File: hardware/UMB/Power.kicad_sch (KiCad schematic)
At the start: 15 parts, among them U3 TLV743P, U4 MC78M12CDTG, U5 LM1117IMP-5.0

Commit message: Power section done
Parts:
- removed C13, C14, C16, C17: 1u, Capacitor_SMD:C_0603_1608Metric_Pad1.08x0.95mm_HandSolder, symbol Device:C
- removed C18: 100n, Capacitor_SMD:C_0603_1608Metric_Pad1.08x0.95mm_HandSolder, symbol Device:C
- removed F1: 500mA, Diode_SMD:D_1812_4532Metric_Pad1.30x3.40mm_HandSolder, symbol Device:Fuse
- removed U4: MC78M12CDTG, Package_TO_SOT_SMD:TO-252-3_TabPin2, symbol mc78m05_to252-regulator_linear:MC78M05_TO252-Regulator_Linear
- removed U5: LM1117IMP-5.0, Package_TO_SOT_SMD:SOT-223-3_TabPin2, symbol lm1117-5.0-regulator_linear:LM1117-5.0-Regulator_Linear
- added C14, C17, C18: 100n, Capacitor_SMD:C_0603_1608Metric_Pad1.08x0.95mm_HandSolder, symbol Device:C_Small
- added C16, C20, C29, C31, C41: 22u, Capacitor_SMD:C_0603_1608Metric_Pad1.08x0.95mm_HandSolder, symbol Device:C_Small
- added C19, C21, C42, C43: 10u, 10uFpolarized_cap:CAPAE660X600N, symbol Device:C_Polarized_Small
- added C22, C24, C26, C27: 2.2u, Capacitor_SMD:C_0805_2012Metric_Pad1.18x1.45mm_HandSolder, symbol Device:C_Small
- added C23: 8.2n, Capacitor_SMD:C_0603_1608Metric_Pad1.08x0.95mm_HandSolder, symbol Device:C_Small
- added C25, C30: 10u, Capacitor_SMD:C_0805_2012Metric_Pad1.18x1.45mm_HandSolder, symbol Device:C_Small
- added C28: 470n, Capacitor_SMD:C_0603_1608Metric_Pad1.08x0.95mm_HandSolder, symbol Device:C_Small
- added L1: 15uH, Inductor_SMD:L_APV_APH1040, symbol Device:L
- added L2: 6.8uH, inductor:VLS5045EX330M, symbol Device:L
- added R10, R13, R56: 10.2k, Resistor_SMD:R_0603_1608Metric_Pad0.98x0.95mm_HandSolder, symbol Device:R_Small
- added R12: 84.5k, Resistor_SMD:R_0603_1608Metric_Pad0.98x0.95mm_HandSolder, symbol Device:R_Small
- added R9: 174k, Resistor_SMD:R_0603_1608Metric_Pad0.98x0.95mm_HandSolder, symbol Device:R_Small
- added U4: TPS563300DRLR, sot-583-8:TPS62932DRLR, symbol TPS563300DRLR:TPS563300DRLR
- added U5: TPS563219ADDFR, SOT65P280X110-8N, symbol TPS563219ADDFR:TPS563219ADDFR
- added U6: AP2127N3-1.5, Package_TO_SOT_SMD:TSOT-23_HandSoldering, symbol Regulator_Linear:AP2127N3-1.5
- added U7: LDK320ADU120R, Package_TO_SOT_SMD:SOT-89-3_Handsoldering, symbol Regulator_Linear:L78L12_SOT89
- added U8: LM2940SX-12_NOPB, KTT0003B, symbol LM2940SX-12_NOPB:LM2940SX-12_NOPB
- added U9: LM1117IMP-5.0, Package_TO_SOT_SMD:SOT-223-3_TabPin2, symbol lm1117-5.0-regulator_linear:LM1117-5.0-Regulator_Linear
- C15: footprint Capacitor_SMD:C_0603_1608Metric -> Capacitor_SMD:C_0603_1608Metric_Pad1.08x0.95mm_HandSolder; Mouser (none) -> https://www.mouser.pl/ProductDetail/KEMET/C0603C104M4RACAUT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; Mouser No (none) -> 80-C0603C104M4RAUTO
- C32: renamed from C19; footprint Capacitor_SMD:C_0603_1608Metric -> Capacitor_SMD:C_0603_1608Metric_Pad1.08x0.95mm_HandSolder; Mouser (none) -> https://www.mouser.pl/ProductDetail/KEMET/C0603C105K4RACTU?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; Mouser No (none) -> 80-C0603C105K4R
- C33: renamed from C20; footprint Capacitor_SMD:C_0603_1608Metric -> Capacitor_SMD:C_0603_1608Metric_Pad1.08x0.95mm_HandSolder; Mouser (none) -> https://www.mouser.pl/ProductDetail/KEMET/C0603C104M4RACAUT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; Mouser No (none) -> 80-C0603C104M4RAUTO
- C34: renamed from C21; footprint Capacitor_SMD:C_0603_1608Metric -> Capacitor_SMD:C_0603_1608Metric_Pad1.08x0.95mm_HandSolder; Mouser (none) -> https://www.mouser.pl/ProductDetail/KEMET/C0603C105K4RACTU?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; Mouser No (none) -> 80-C0603C105K4R
- U10: renamed from U3; Mouser (none) -> 595-TLV74333PDBVR
- renumbered D24 to D1, TP11 to TP1
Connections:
- net +12V: now also C29.1, U8.3 (OUT); no longer C15.1
- net +24V: now also C15.1, D1.2 (A2), C21.1, U4.3 (VIN)
- net +5V: now also C31.1, U9.2 (VO); no longer C32.1, U10.1 (IN), U10.3 (EN)
- net AGND renamed GND
- net GND: now also C16.2, C18.2, C19.2, C20.2, C21.2, C22.2, C23.2, C24.2, C25.2, C26.2, C27.2, C28.2, C29.2, C30.2, C31.2, C41.2, C42.2, C43.2, R10.2, R13.2, U4.4 (GND), U5.1 (GND), U6.1 (GND), U7.2 (GND), U8.2 (GND), U9.1 (GND)
- new net: R10.1, R9.1, U4.8 (FB)
- new net: C17.2, L2.1, U5.2 (SW)
- new net: R12.2, R13.1, U5.6 (VFB)
- new net: C17.1, U5.8 (VBST)
- new net: C14.1, L1.1, U4.5 (SW)
- new net: C14.2, U4.6 (BST)
- new net: C23.1, U5.5 (SS)
- new net: R56.2, U5.7 (EN)
- new net +12VA: C27.1, U7.1 (OUT)
- new net +14.5V: C16.1, C18.1, C19.1, C26.1, C28.1, C41.1, C42.1, L1.2, R56.1, R9.2, U5.3 (VIN), U7.3 (IN), U8.1 (IN)
- new net +5VA: C22.1, C25.1, U6.2 (VO)
- new net +7V: C20.1, C24.1, C30.1, C32.1, C43.1, L2.2, R12.1, U10.1 (IN), U10.3 (EN), U6.3 (VI), U9.3 (VI)
- no-connect marks 0 -> 4
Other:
- note added: "+12V"
- note added: "+12VA"
- note added: "+3V3"
- note added: "+5V"
- note added: "+5VA"
- note added: "12V LDO"
- note added: "14.5V DC/DC"
- note added: "24VIN"
- note added: "3V3 LDO"
- note added: "5V LDO"
- note added: "7V DC/DC"
- note added: "ANALOG"
- note added: "DIGITAL & SENSORS"
- note added: "Power Section Diagram"
- moved on the sheet: C32, C33, C34, D1, TP1, U10

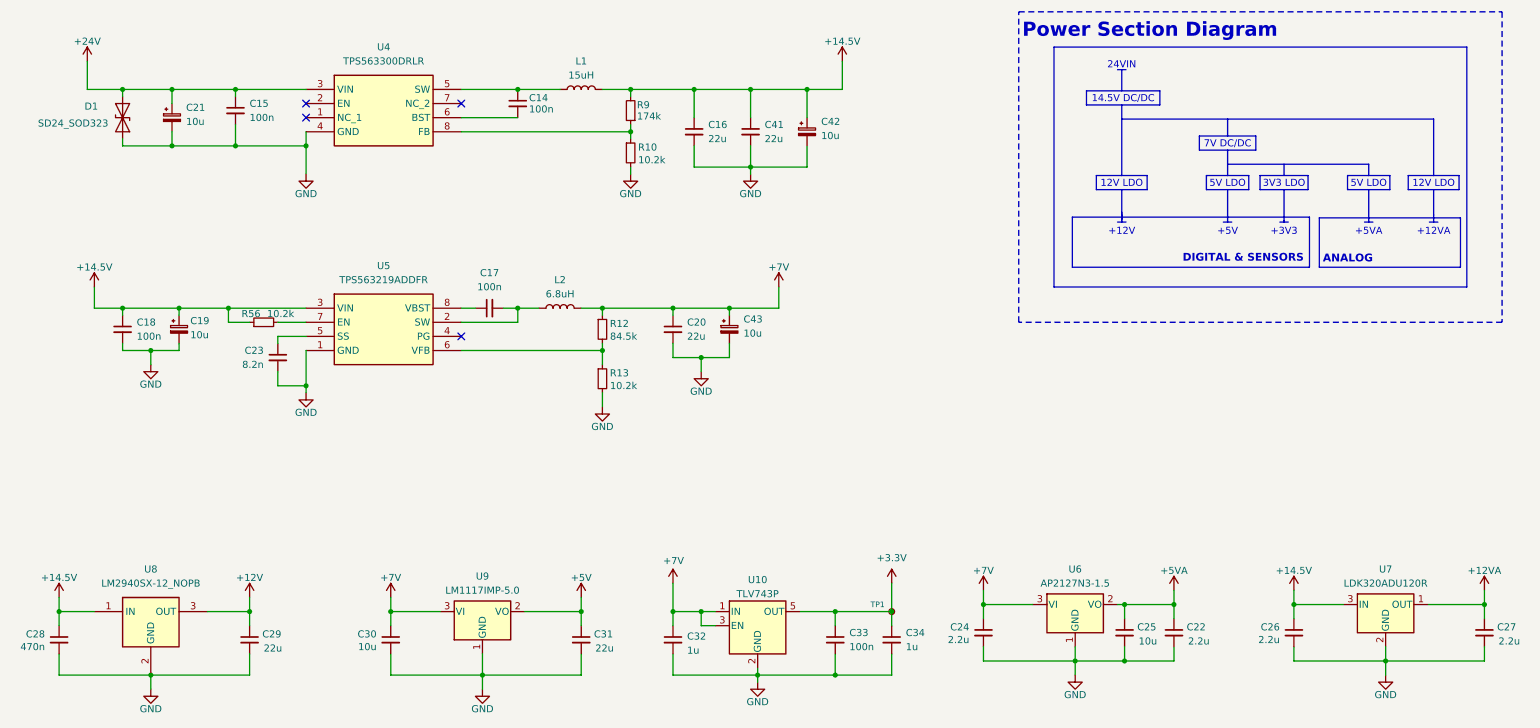
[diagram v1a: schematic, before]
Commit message: Added all footprints and parts Mouser IDs
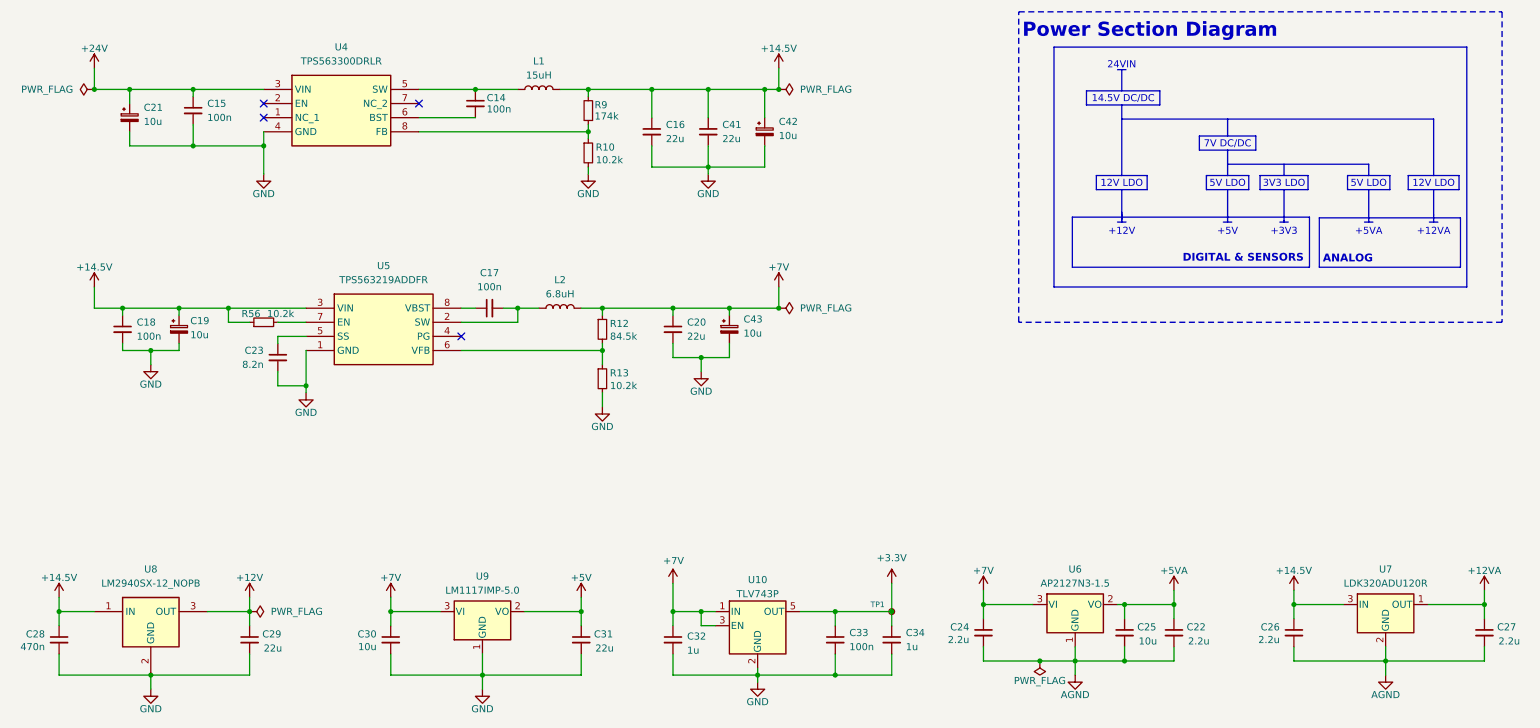
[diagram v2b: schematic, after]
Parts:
- removed D1: SD24_SOD323, Diode_SMD:D_SOD-323, symbol Diode:SD24_SOD323
- C14, C15, C17, C18, C33: Manufacturer_Part_Number (none) -> C0603C104M4RACAUTO
- C16, C20, C29, C31, C41: Manufacturer_Part_Number (none) -> CC1210KKX7R8BB226
- C19, C21, C42, C43: Manufacturer_Part_Number (none) -> A767EB106M1VLAE085
- C22, C24, C26, C27: Manufacturer_Part_Number (none) -> TMCP1A475KTRF
- C23: Manufacturer_Part_Number (none) -> C0402C103K1RACAUTO7411
- C25, C30: Manufacturer_Part_Number (none) -> TL8W9226M010C
- C28: Manufacturer_Part_Number (none) -> GRT188R61H105KE13D
- C32, C34: Manufacturer_Part_Number (none) -> C0603C105K4RACTU
- L1, L2: Manufacturer_Part_Number (none) -> 104CDMCCDS-150MC
- R10, R13, R56: Manufacturer_Part_Number (none) -> RT0603FRE0710K2L; Mouser No (none) -> 603-RT0603FRE0710K2L; Mouser Part Number 603-RT0603FRE0710K2L -> (none)
- R12: Manufacturer_Part_Number (none) -> RT0603FRE0784K5L; Mouser No (none) -> 603-RT0603FRE0784K5L; Mouser Part Number 603-RT0603FRE0784K5L -> (none)
- R9: Manufacturer_Part_Number (none) -> RT0603FRE07174KL; Mouser No (none) -> 603-RT0603FRE07174KL; Mouser Part Number 603-RT0603FRE07174KL -> (none)
- U10: Manufacturer_Part_Number (none) -> TLV74333PDBVR; Mouser 595-TLV74333PDBVR -> https://www.mouser.pl/ProductDetail/Texas-Instruments/TLV74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; Mouser No (none) -> 595-TLV74333PDBVR
- U4: Height 0.6 -> (none); Manufacturer_Name Texas Instruments -> (none); Mouser (none) -> https://www.mouser.pl/ProductDetail/Texas-Instruments/TPS56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; Mouser No (none) -> 595-TPS563300DRLR; Mouser Part Number 595-TPS563300DRLR -> (none); Mouser Price/Stock https://www.mouser.co.uk/ProductDetail/Texas-Instruments/TP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 -> (none)
- U5: Height 1.1 -> (none); Manufacturer_Name Texas Instruments -> (none); Mouser (none) -> https://www.mouser.pl/ProductDetail/Texas-Instruments/TPS56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; Mouser No (none) -> 595-TPS563219ADDFR; Mouser Part Number 595-TPS563219ADDFR -> (none); Mouser Price/Stock https://www.mouser.co.uk/ProductDetail/Texas-Instruments/TP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 -> (none)
- U6: Manufacturer_Part_Number (none) -> AP7375-50SA-7; Mouser 621-AP7375-50SA-7 -> https://www.mouser.pl/ProductDetail/Diodes-Incorporated/AP7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; Mouser No (none) -> 621-AP7375-50SA-7
- U7: Manufacturer_Part_Number (none) -> LDK320ADU120R; Mouser 511-LDK320ADU120R -> https://www.mouser.pl/ProductDetail/STMicroelectronics/LDK3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; Mouser No (none) -> 511-LDK320ADU120R
- U8: Manufacturer_Name Texas Instruments -> (none); Mouser (none) -> https://www.mouser.pl/ProductDetail/Texas-Instruments/LM294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; Mouser No (none) -> 926-LM2940SX-12/NOPB; Mouser Part Number 926-LM2940SX-12/NOPB -> (none); Mouser Price/Stock https://www.mouser.co.uk/ProductDetail/Texas-Instruments/LM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 -> (none)
- U9: Manufacturer_Part_Number (none) -> LM1117IMP-5.0/NOPB; Mouser (none) -> https://www.mouser.pl/ProductDetail/Texas-Instruments/LM111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; Mouser No (none) -> 926-LM1117IMP5.0NOPB; Mouser# 926-LM1117IMPX50NOPB -> (none)
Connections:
- net GND: no longer C22.2, C24.2, C25.2, C26.2, C27.2, U6.1 (GND), U7.2 (GND)
- new net AGND: C22.2, C24.2, C25.2, C26.2, C27.2, U6.1 (GND), U7.2 (GND)
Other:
- moved on the sheet: C14, C15, C16, C21, C41, C42, L1, R10, R9, U4
